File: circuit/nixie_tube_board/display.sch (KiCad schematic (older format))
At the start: 10 parts, among them P5 CONN_01X08, P6 CONN_01X12, U10 IN-14, U11 IN-14, U12 IN-14, U13 IN-14, U14 IN-14, U15 IN-14, U16 IN-14, U17 IN-14

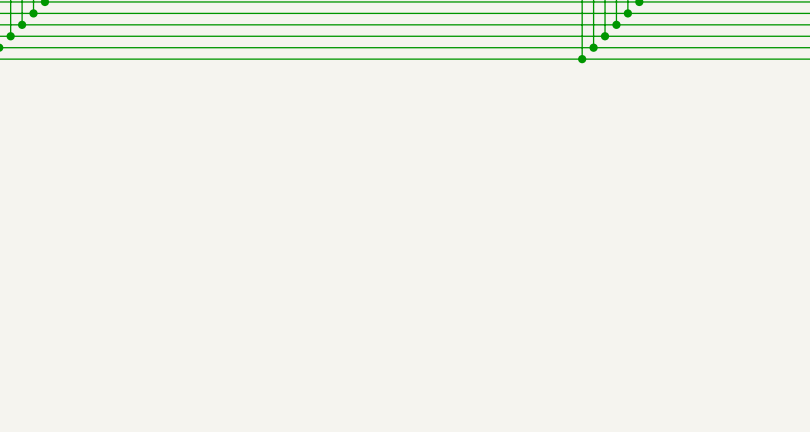
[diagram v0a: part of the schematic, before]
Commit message: New hardware is almost finished
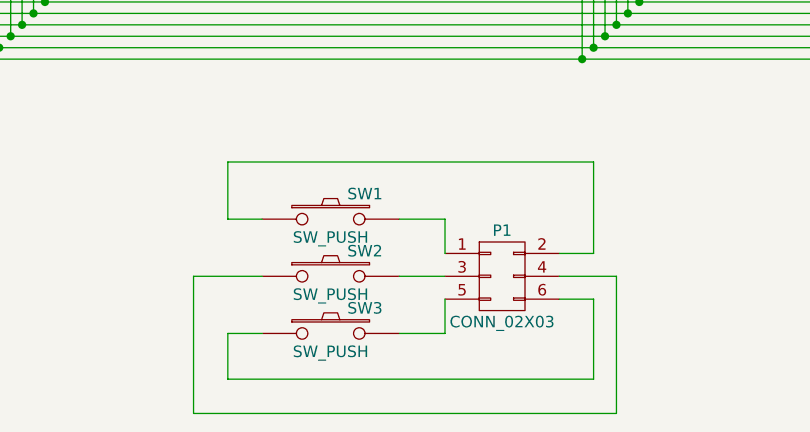
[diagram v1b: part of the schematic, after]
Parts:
- added P1: CONN_02X03, SMD_PIN_2_BY_3:SMD_PIN_2_BY_3, symbol CONN_02X03
- added SW1, SW2, SW3: SW_PUSH, Buttons_Switches_ThroughHole:SW_PUSH-12mm, symbol SW_PUSH
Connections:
- new net: P1.2 (P2), SW1.1
- new net: P1.1 (P1), SW1.2
- new net: P1.4 (P4), SW2.1
- new net: P1.3 (P3), SW2.2
- new net: P1.6 (P6), SW3.1
- new net: P1.5 (P5), SW3.2
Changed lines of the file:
@@
 Connection ~ 10700 4250
 Connection ~ 10700 1750
+$Comp
+L SW_PUSH SW1
+U 1 1 573D27B7
+P 4850 6550
+F 0 "SW1" H 5000 6660 50  0000 C CNN
+F 1 "SW_PUSH" H 4850 6470 50  0000 C CNN
+F 2 "Buttons_Switches_ThroughHole:SW_PUSH-12mm" H 4850 6550 50  0001 C CNN
+F 3 "" H 4850 6550 50  0000 C CNN
+	1    4850 6550
+	1    0    0    -1
+$EndComp
+$Comp
+L SW_PUSH SW2
+U 1 1 573D2802
+P 4850 6800
+F 0 "SW2" H 5000 6910 50  0000 C CNN
+F 1 "SW_PUSH" H 4850 6720 50  0000 C CNN
+F 2 "Buttons_Switches_ThroughHole:SW_PUSH-12mm" H 4850 6800 50  0001 C CNN
+F 3 "" H 4850 6800 50  0000 C CNN
+	1    4850 6800
+	1    0    0    -1
+$EndComp
+$Comp
+L SW_PUSH SW3
+U 1 1 573D2843
+P 4850 7050
+F 0 "SW3" H 5000 7160 50  0000 C CNN
+F 1 "SW_PUSH" H 4850 6970 50  0000 C CNN
+F 2 "Buttons_Switches_ThroughHole:SW_PUSH-12mm" H 4850 7050 50  0001 C CNN
+F 3 "" H 4850 7050 50  0000 C CNN
+	1    4850 7050
+	1    0    0    -1
+$EndComp
+$Comp
+L CONN_02X03 P1
+U 1 1 573D2ACB
+P 5600 6800
+F 0 "P1" H 5600 7000 50  0000 C CNN
+F 1 "CONN_02X03" H 5600 6600 50  0000 C CNN
+F 2 "SMD_PIN_2_BY_3:SMD_PIN_2_BY_3" H 5600 5600 50  0001 C CNN
+F 3 "" H 5600 5600 50  0000 C CNN
+	1    5600 6800
+	1    0    0    -1
+$EndComp
+Wire Wire Line
+	5150 6800 5350 6800
+Wire Wire Line
+	5150 6550 5350 6550
+Wire Wire Line
+	5350 6550 5350 6700
+Wire Wire Line
+	5150 7050 5350 7050
+Wire Wire Line
+	5350 7050 5350 6900
+Wire Wire Line
+	5850 6700 6000 6700
+Wire Wire Line
+	6000 6700 6000 6300
+Wire Wire Line
+	6000 6300 4400 6300
+Wire Wire Line
+	4400 6300 4400 6550
+Wire Wire Line
+	4400 6550 4550 6550
+Wire Wire Line
+	5850 6900 6000 6900
+Wire Wire Line
+	6000 6900 6000 7250
+Wire Wire Line
+	6000 7250 4400 7250
+Wire Wire Line
+	4400 7250 4400 7050
+Wire Wire Line
+	4400 7050 4550 7050
+Wire Wire Line
+	5850 6800 6100 6800
+Wire Wire Line
+	6100 6800 6100 7400
+Wire Wire Line
+	6100 7400 4250 7400
+Wire Wire Line
+	4250 7400 4250 6800
+Wire Wire Line
+	4250 6800 4550 6800
 $EndSCHEMATC
